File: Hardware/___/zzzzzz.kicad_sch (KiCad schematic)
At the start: 9 parts, among them J1 Conn_01x07_Male, J2 Conn_01x04_Male, J3 Conn_01x02_Male, J4 Conn_01x02_Male, J5 Conn_01x02_Male, J6 Conn_01x02_Male, J7 Conn_01x08_Male, J8 Conn_01x08_Male, J9 QWIIC_Stackable

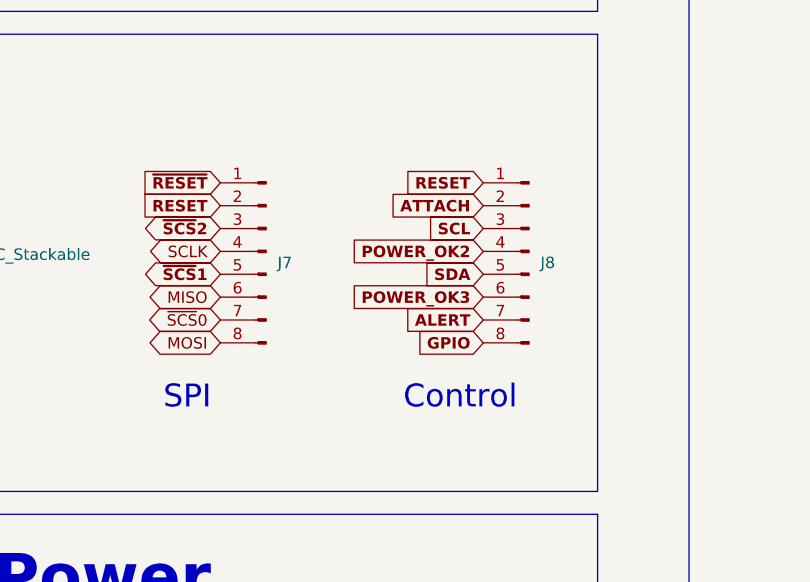
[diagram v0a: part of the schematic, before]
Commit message: Working on Controller-Tarduino Clone
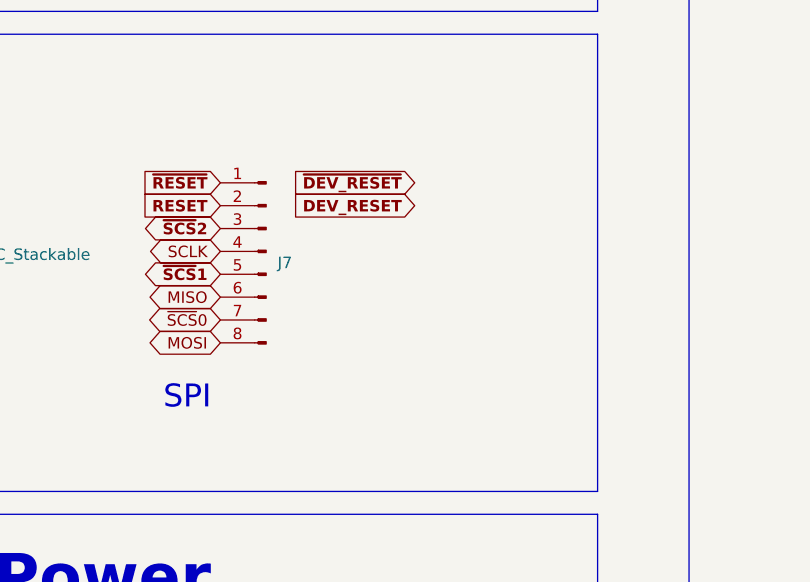
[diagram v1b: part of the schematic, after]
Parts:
- removed J8: Conn_01x08_Male, Tinker:PinHeader_2x04_P1.27mm_Vertical, symbol Connector:Conn_01x08_Male
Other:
- note removed: "Control"

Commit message: Working on the RP2040 & cleaning up stuff...
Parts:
- added J8: QWIIC_Vertical, Tinker:QWIIC_Vertical, symbol Connector_Generic_MountingPin:Conn_01x04_MountingPin
- J9: value QWIIC_Stackable -> QWIIC_Stack_II
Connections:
- net +3V3: now also J8.2 (Pin_2)
- net GND: now also J8.1 (Pin_1), J8.MP (MountPin)
- net SCL: now also J8.4 (Pin_4)
- net SDA: now also J8.3 (Pin_3)
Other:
- note added: "Stackable QWIIC"
- note added: "Vertical QWIIC"
- moved on the sheet: J1, J2, J3, J4, J5, J6, J7, J9
